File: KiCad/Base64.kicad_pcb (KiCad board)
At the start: 4 copper layers, 25.1 x 81.8 mm, 2 parts, among them J1 1473149-1, U1 68000D

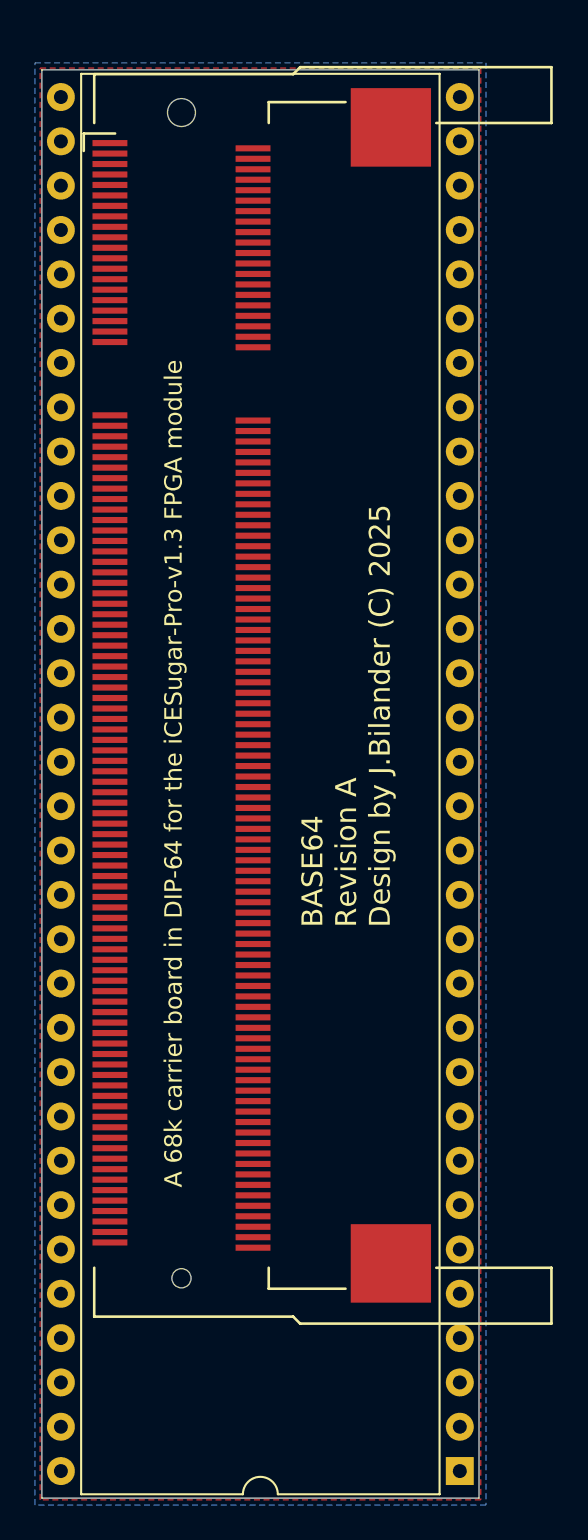
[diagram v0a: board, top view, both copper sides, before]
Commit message: more placement and routing
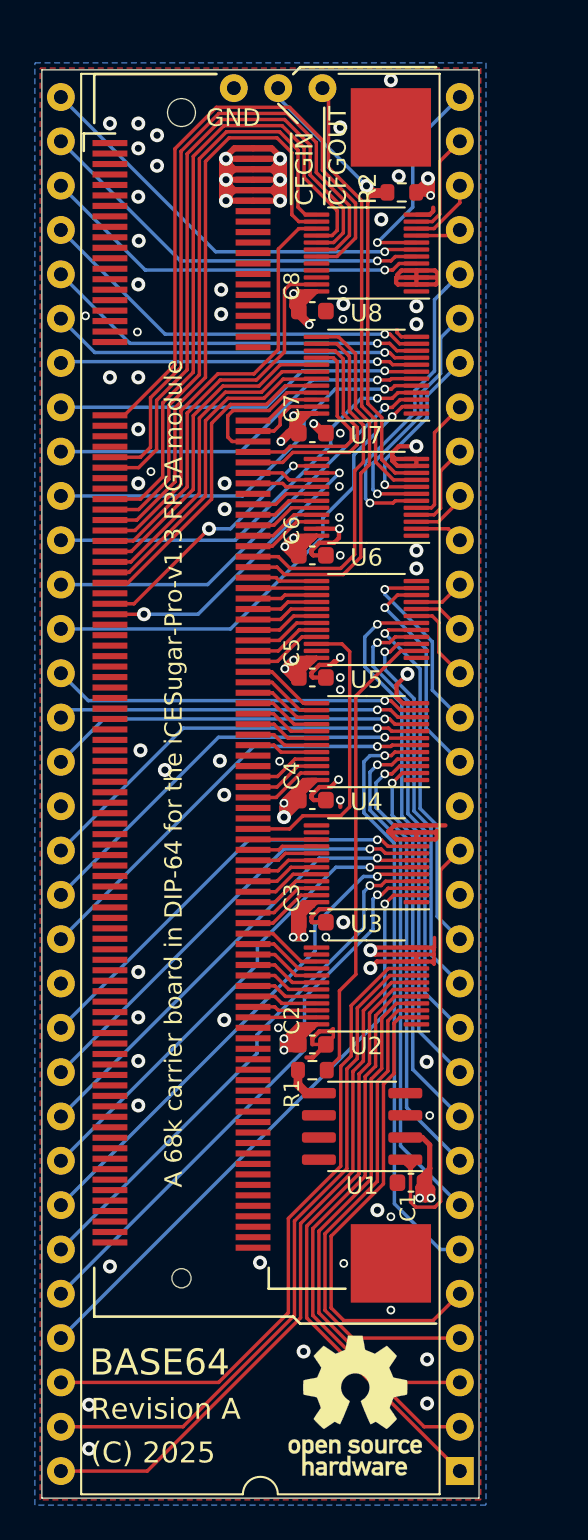
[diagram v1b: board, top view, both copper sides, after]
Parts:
- added C1: 10nF, Capacitor_SMD:C_0603_1608Metric, F.Cu at (110.5, 107.2)
- added C2: 100nF, Capacitor_SMD:C_0603_1608Metric, F.Cu at (104.8, 99.3)
- added C3: 100nF, Capacitor_SMD:C_0603_1608Metric, F.Cu at (104.8, 92.3)
- added C4: 100nF, Capacitor_SMD:C_0603_1608Metric, F.Cu at (104.8, 85.3)
- added C5: 100nF, Capacitor_SMD:C_0603_1608Metric, F.Cu at (104.8, 78.3)
- added C6: 100nF, Capacitor_SMD:C_0603_1608Metric, F.Cu at (104.8, 71.3)
- added C7: 100nF, Capacitor_SMD:C_0603_1608Metric, F.Cu at (104.8, 64.3)
- added C8: 100nF, Capacitor_SMD:C_0603_1608Metric, F.Cu at (104.8, 57.3)
- added J2: Conn_01x03, Connector_PinHeader_2.54mm:PinHeader_1x03_P2.54mm_Horizontal, B.Cu at (105.4, 44.5)
- added R1: 33, Resistor_SMD:R_0603_1608Metric, F.Cu at (104.8, 100.8)
- added R2: R_Small, Resistor_SMD:R_0603_1608Metric, F.Cu at (110.0, 50.5)
- added REF**: OSHW-Logo_7.5x8mm_SilkScreen, Symbol:OSHW-Logo_7.5x8mm_SilkScreen, F.Cu at (107.3, 120.0)
- added REF**: Symbol_CC-Attribution_SilkScreenTop_Small, SF2000:Symbol_CC-Attribution_SilkScreenTop_Small, B.Cu at (101.9, 54.0)
- added REF**: Symbol_CC_SilkScreenTop_Small, SF2000:Symbol_CC_SilkScreenTop_Small, B.Cu at (108.7, 54.0)
- added REF**: Symbol_CC-ShareAlike_SilkScreenTop_Small, SF2000:Symbol_CC-ShareAlike_SilkScreenTop_Small, B.Cu at (95.1, 54.0)
- added REF**: OSHW-Logo_11.4x12mm_SilkScreen, Symbol:OSHW-Logo_11.4x12mm_SilkScreen, B.Cu at (101.9, 112.5)
- added U1: 501MLFT, Package_SO:SOIC-8_3.9x4.9mm_P1.27mm, F.Cu at (107.7, 104.0)
- added U2: SN74CBTD3861DGVR, Package_SO:TSSOP-24_4.4x5mm_P0.4mm, F.Cu at (108.0, 96.0)
- added U3: SN74CBTD3861DGVR, Package_SO:TSSOP-24_4.4x5mm_P0.4mm, F.Cu at (108.0, 89.0)
- added U4: SN74CBTD3861DGVR, Package_SO:TSSOP-24_4.4x5mm_P0.4mm, F.Cu at (108.0, 82.0)
- added U5: SN74CBTD3861DGVR, Package_SO:TSSOP-24_4.4x5mm_P0.4mm, F.Cu at (108.0, 75.0)
- added U6: SN74CBTD3861DGVR, Package_SO:TSSOP-24_4.4x5mm_P0.4mm, F.Cu at (108.0, 68.0)
- added U7: SN74CBTD3861DGVR, Package_SO:TSSOP-24_4.4x5mm_P0.4mm, F.Cu at (108.0, 61.0)
- added U8: SN74CBTD3861DGVR, Package_SO:TSSOP-24_4.4x5mm_P0.4mm, F.Cu at (108.0, 54.0)
- U9: renamed from U1; value 68000D -> 68000_PinHeader
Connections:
- net Net-(J1-Pad101) renamed PL20B
- net Net-(J1-Pad103) renamed PL23A
- net Net-(J1-Pad109) renamed PL23B
- net Net-(J1-Pad111) renamed PL23C
- net Net-(J1-Pad113) renamed PL23D
- net Net-(J1-Pad115) renamed PL26A
- net Net-(J1-Pad116) renamed PT33B
- net Net-(J1-Pad117) renamed PL26B
- net Net-(J1-Pad118) renamed PT27A
- net Net-(J1-Pad119) renamed PL26C
- net Net-(J1-Pad121) renamed PL26D
- net Net-(J1-Pad123) renamed PL32A
- net Net-(J1-Pad125) renamed PL35D
- net Net-(J1-Pad127) renamed PL35A
- net Net-(J1-Pad129) renamed PL32B
- net Net-(J1-Pad131) renamed PL35B
- net Net-(J1-Pad133) renamed PL38C
- net Net-(J1-Pad135) renamed PL38D
- net Net-(J1-Pad137) renamed PL41B
- net Net-(J1-Pad139) renamed PL41D
- net Net-(J1-Pad141) renamed PL41C
- net Net-(J1-Pad143) renamed PL44B
- net Net-(J1-Pad145) renamed PL44A
- net Net-(J1-Pad147) renamed PB4B
- net Net-(J1-Pad149) renamed PB4A
- net Net-(J1-Pad151) renamed PB6B
- net Net-(J1-Pad153) renamed PB6A
- net Net-(J1-Pad155) renamed PB13A
- net Net-(J1-Pad75) renamed PT4A
- net Net-(J1-Pad81) renamed PL5A
- net Net-(J1-Pad83) renamed PL5B
- net Net-(J1-Pad85) renamed PL8A
- net Net-(J1-Pad87) renamed PL2D
- net Net-(J1-Pad89) renamed PL11D
- net Net-(J1-Pad91) renamed PL8B
- net Net-(J1-Pad93) renamed PL14A
- net Net-(J1-Pad95) renamed PL11C
- net Net-(J1-Pad97) renamed PL20A
- net Net-(J1-Pad99) renamed PL14B
- J1 pad 1: Net-(J1-Pad1) -> GND
- J1 pad 10: Net-(J1-Pad10) -> VCC
- J1 pad 100: Net-(J1-Pad100) -> PT51A
- J1 pad 102: Net-(J1-Pad102) -> PT44B
- J1 pad 104: Net-(J1-Pad104) -> PT47A
- J1 pad 105: Net-(J1-Pad105) -> GND
- J1 pad 106: Net-(J1-Pad106) -> GND
- J1 pad 107: Net-(J1-Pad107) -> GND
- J1 pad 108: Net-(J1-Pad108) -> GND
- J1 pad 11: Net-(J1-Pad11) -> GND
- J1 pad 110: Net-(J1-Pad110) -> PT38B
- J1 pad 112: Net-(J1-Pad112) -> PT40A
- J1 pad 114: Net-(J1-Pad114) -> PT35A
- J1 pad 12: Net-(J1-Pad12) -> VCC
- J1 pad 120: Net-(J1-Pad120) -> PT24B
- J1 pad 122: Net-(J1-Pad122) -> PT22A
- J1 pad 124: Net-(J1-Pad124) -> PT20B
- J1 pad 126: Net-(J1-Pad126) -> PT15A
- J1 pad 128: Net-(J1-Pad128) -> PT13B
- J1 pad 130: Net-(J1-Pad130) -> PT11A
- J1 pad 132: Net-(J1-Pad132) -> PT9B
- J1 pad 134: Net-(J1-Pad134) -> PL2C
- J1 pad 136: Net-(J1-Pad136) -> PT9A
- J1 pad 138: Net-(J1-Pad138) -> PL5C
- J1 pad 140: Net-(J1-Pad140) -> PL8C
- J1 pad 142: Net-(J1-Pad142) -> PL5D
- J1 pad 144: Net-(J1-Pad144) -> PL11B
- J1 pad 146: Net-(J1-Pad146) -> PL14C
- J1 pad 148: Net-(J1-Pad148) -> PL14D
- J1 pad 150: Net-(J1-Pad150) -> PL17C
- J1 pad 152: Net-(J1-Pad152) -> PL20C
- J1 pad 154: Net-(J1-Pad154) -> PL29A
- J1 pad 156: Net-(J1-Pad156) -> PL20D
- J1 pad 157: Net-(J1-Pad157) -> GND
- J1 pad 158: Net-(J1-Pad158) -> GND
- J1 pad 199: Net-(J1-Pad199) -> GND
- J1 pad 2: Net-(J1-Pad2) -> VCC
- J1 pad 200: Net-(J1-Pad200) -> GND
- J1 pad 3: Net-(J1-Pad3) -> GND
- J1 pad 39: Net-(J1-Pad39) -> GND
- J1 pad 4: Net-(J1-Pad4) -> VCC
- J1 pad 40: Net-(J1-Pad40) -> GND
- J1 pad 41: Net-(J1-Pad41) -> PT29B
- J1 pad 42: Net-(J1-Pad42) -> PR47C
- J1 pad 44: Net-(J1-Pad44) -> PR47D
- J1 pad 46: Net-(J1-Pad46) -> PR44D
- J1 pad 48: Net-(J1-Pad48) -> PR41A
- J1 pad 49: Net-(J1-Pad49) -> PT35B
- J1 pad 5: Net-(J1-Pad5) -> GND
- J1 pad 50: Net-(J1-Pad50) -> PR38A
- J1 pad 51: Net-(J1-Pad51) -> PT29A
- J1 pad 52: Net-(J1-Pad52) -> PR38B
- J1 pad 54: Net-(J1-Pad54) -> PR44C
- J1 pad 55: Net-(J1-Pad55) -> GND
- J1 pad 56: Net-(J1-Pad56) -> GND
- J1 pad 57: Net-(J1-Pad57) -> PT27B
- J1 pad 58: Net-(J1-Pad58) -> PR35C
- J1 pad 59: Net-(J1-Pad59) -> PT18B
- J1 pad 6: Net-(J1-Pad6) -> VCC
- J1 pad 60: Net-(J1-Pad60) -> PR32C
- J1 pad 61: Net-(J1-Pad61) -> PT22B
- J1 pad 62: Net-(J1-Pad62) -> PR29C
- J1 pad 63: Net-(J1-Pad63) -> PT18A
- J1 pad 64: Net-(J1-Pad64) -> PR20D
- J1 pad 65: Net-(J1-Pad65) -> PT15B
- J1 pad 66: Net-(J1-Pad66) -> PR29A
- J1 pad 67: Net-(J1-Pad67) -> PT6B
- J1 pad 68: Net-(J1-Pad68) -> PR20C
- J1 pad 69: Net-(J1-Pad69) -> PT11B
- J1 pad 7: Net-(J1-Pad7) -> GND
- J1 pad 70: Net-(J1-Pad70) -> PR17C
- J1 pad 71: Net-(J1-Pad71) -> PT6A
- J1 pad 72: Net-(J1-Pad72) -> PR14D
- J1 pad 73: Net-(J1-Pad73) -> PT4B
- J1 pad 74: Net-(J1-Pad74) -> PR17B
- J1 pad 76: Net-(J1-Pad76) -> PR14C
- J1 pad 77: Net-(J1-Pad77) -> PL2A
- J1 pad 78: Net-(J1-Pad78) -> PR11B
- J1 pad 79: Net-(J1-Pad79) -> PL2B
- J1 pad 8: Net-(J1-Pad8) -> VCC
- J1 pad 80: Net-(J1-Pad80) -> PR5D
- J1 pad 82: Net-(J1-Pad82) -> PR8C
- J1 pad 84: Net-(J1-Pad84) -> PR5C
- J1 pad 86: Net-(J1-Pad86) -> PT62B
- J1 pad 88: Net-(J1-Pad88) -> PT58B
- J1 pad 9: Net-(J1-Pad9) -> GND
- J1 pad 90: Net-(J1-Pad90) -> PT62D
- J1 pad 92: Net-(J1-Pad92) -> PT62A
- J1 pad 94: Net-(J1-Pad94) -> PT58D
- J1 pad 96: Net-(J1-Pad96) -> PT58A
- J1 pad 98: Net-(J1-Pad98) -> PT49B
- J1 pad MP1: Net-(J1-PadMP1) -> GND
- J1 pad MP2: Net-(J1-PadMP2) -> GND
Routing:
- net VCC: track 0.00 -> 121.7 mm, vias 0 -> 24
- net GND: track 0.00 -> 65.2 mm, vias 0 -> 71
- net D5: track 0.00 -> 40.2 mm
- net D6: track 0.00 -> 39.3 mm
- net D7: track 0.00 -> 38.4 mm
- net PT35B: track 0.00 -> 37.9 mm
- net PT27B: track 0.00 -> 37.1 mm
- net PT29A: track 0.00 -> 36.8 mm
- net PT29B: track 0.00 -> 36.6 mm
- net PT22B: track 0.00 -> 34.7 mm
- net D4: track 0.00 -> 34.6 mm
- net D8: track 0.00 -> 34.6 mm, vias 0 -> 1
- net PT18B: track 0.00 -> 34.4 mm
- net AS: track 0.00 -> 34.1 mm, vias 0 -> 1
- net D9: track 0.00 -> 32.8 mm, vias 0 -> 1
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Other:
- board text added: "(C) 2025"
- board text added: "BASE64"
- board text added: "CC BY-SA 4.0"
- board text added: "Design by J.Bilander"
- board text added: "GND"
- board text added: "JLCJLCJLCJLC"
- board text added: "Revision A"
- board text added: "~CFGIN"
- board text added: "~CFGOUT"
- board text removed: "BASE64 Revision A Design by J.Bilander (C) 2025"

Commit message: silkscreen fixes, adding a dot to indicate pin 1 on all IC footprints
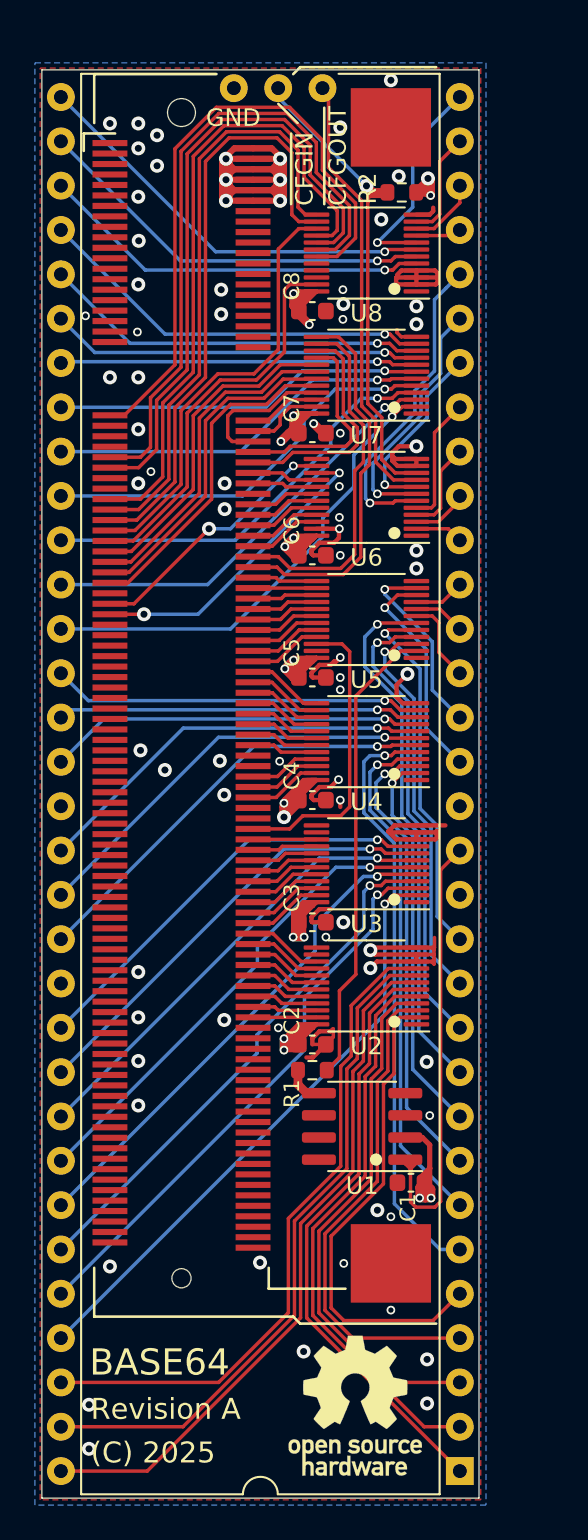
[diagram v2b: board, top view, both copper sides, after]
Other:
- board text removed: "A 68k carrier board in DIP-64 for the iCESugar-Pro-v1.3 FPGA module"

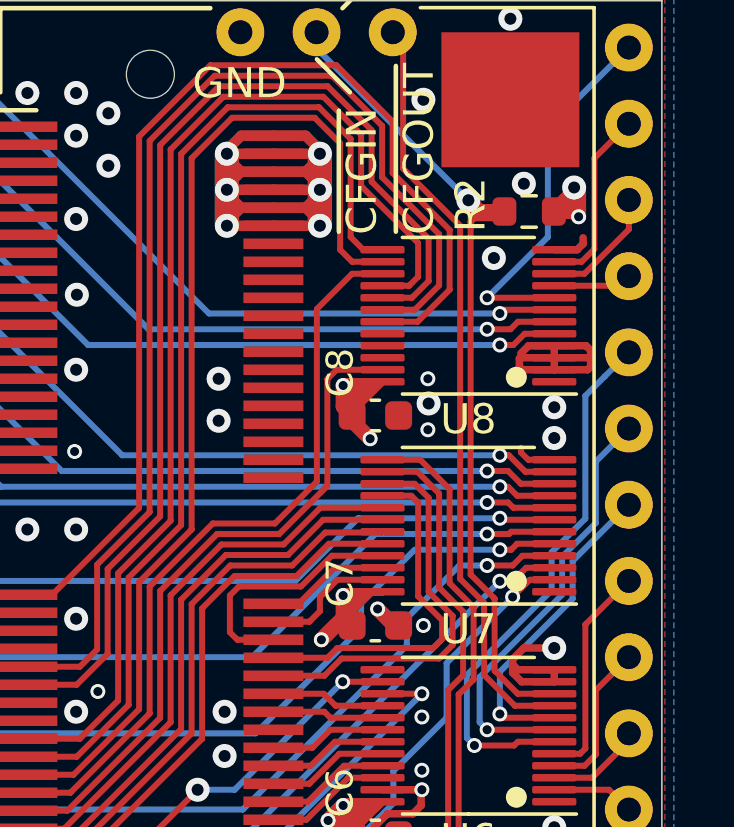
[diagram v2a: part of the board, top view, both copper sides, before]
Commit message: Add value (10k) to R2 pull-up resistor and some small routing improvements
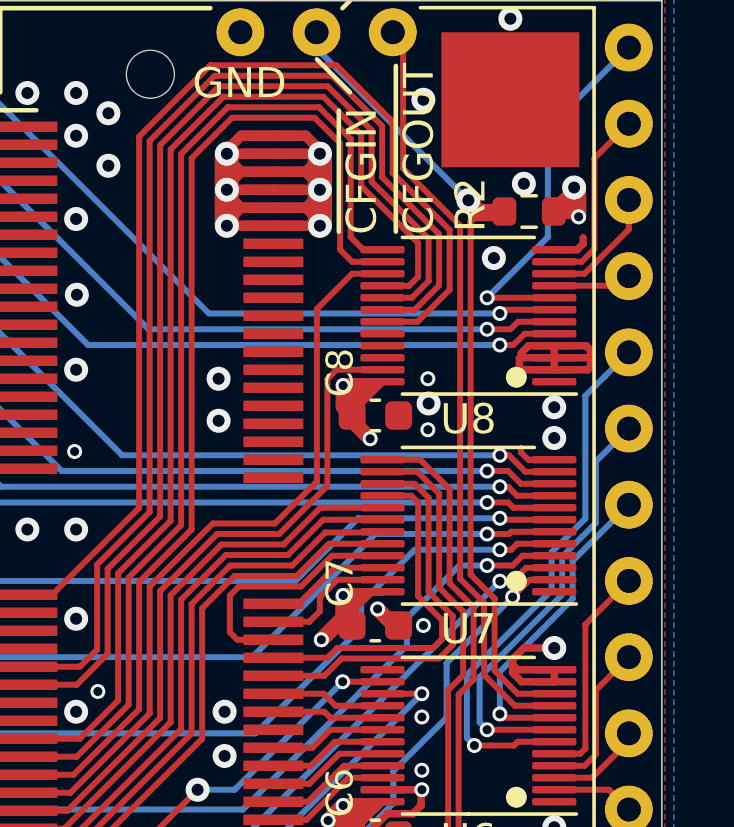
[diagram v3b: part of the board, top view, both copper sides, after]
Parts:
- R2: value R_Small -> 10k
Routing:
- net VCC: track 121.7 -> 124.5 mm
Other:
- rule via_min_size: 0.4 -> 0.5
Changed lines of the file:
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@@
     (thickness 1.6)
     (drawings 18)
-    (tracks 1173)
+    (tracks 1177)
     (zones 0)
     (modules 26)
@@
   )
   (setup
-    (last_trace_width 0.1524)
+    (last_trace_width 0.5)
     (user_trace_width 0.2)
     (user_trace_width 0.25)
@@
     (via_size 0.8)
     (via_drill 0.4)
-    (via_min_size 0.4)
+    (via_min_size 0.5)
     (via_min_drill 0.25)
     (user_via 0.4 0.25)
@@
     (uvia_drill 0.1)
     (uvias_allowed no)
-    (uvia_min_size 0.2)
+    (uvia_min_size 0.3)
     (uvia_min_drill 0.1)
     (edge_width 0.05)
@@
       (effects (font (size 1 1) (thickness 0.15)))
     )
-    (fp_text value R_Small (at 0 1.43) (layer F.Fab) hide
+    (fp_text value 10k (at 0 1.43) (layer F.Fab) hide
       (effects (font (size 1 1) (thickness 0.15)))
     )
@@
   (segment (start 111.625 50.65) (end 111.625 49.825) (width 0.5) (layer F.Cu) (net 2))
   (segment (start 103.275 70.775) (end 103.775 70.275) (width 0.5) (layer B.Cu) (net 2))
+  (segment (start 111.625 49.825) (end 111.475 49.675) (width 0.5) (layer B.Cu) (net 2))
+  (segment (start 111.625 50.65) (end 111.625 49.825) (width 0.5) (layer B.Cu) (net 2))
+  (segment (start 103.775 64.025) (end 103.05 64.75) (width 0.5) (layer B.Cu) (net 2))
+  (segment (start 103.775 63.275) (end 103.775 64.025) (width 0.5) (layer B.Cu) (net 2))
   (via (at 108.575 53.35) (size 0.5) (drill 0.3) (layers F.Cu B.Cu) (net 3))
   (segment (start 110.8125 53.35) (end 108.575 53.35) (width 0.2) (layer F.Cu) (net 3))

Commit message: Fixed typo on CFGOUT net and corrected signal direction on many nets
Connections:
- net CFOUT renamed CFGOUT

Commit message: Small silkscreen fix on underside
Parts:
- moved REF** 0.20 mm to (101.9, 53.8)
- moved REF** 0.20 mm to (108.7, 53.8)
- moved REF** 0.20 mm to (95.1, 53.8)

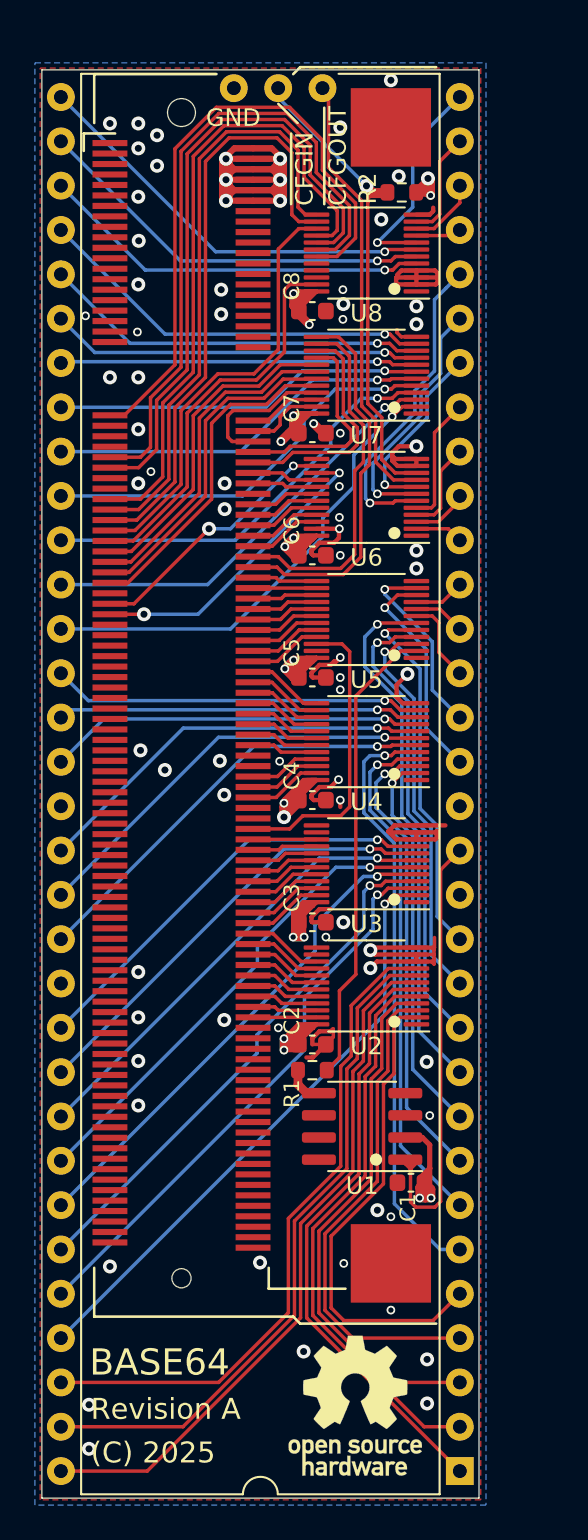
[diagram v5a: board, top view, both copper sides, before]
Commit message: Add a 74AHCT1G17 buffering the raw 7 MHz clk and fanout to the 501 PLL (U1) and a pin in the CBTD (U6) that propagates to PL23A (J1 on the FPGA)
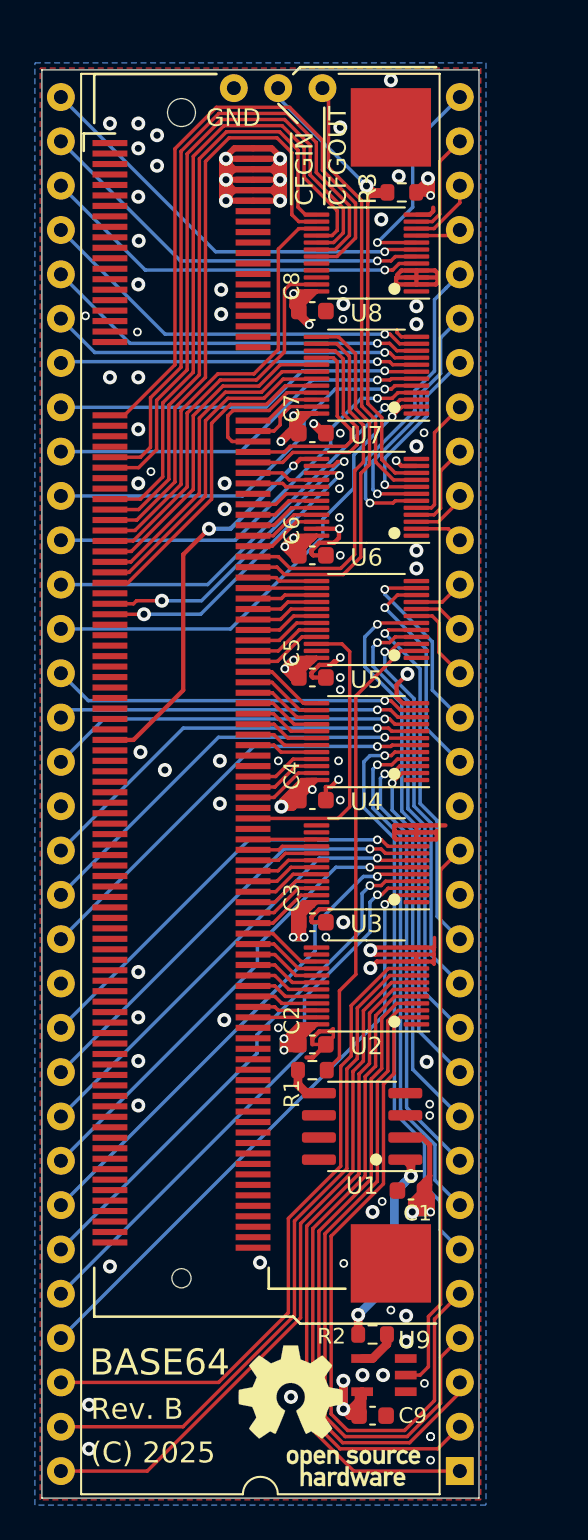
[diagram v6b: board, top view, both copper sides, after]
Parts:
- added C9: 100nF, Capacitor_SMD:C_0603_1608Metric, F.Cu at (108.3, 120.6)
- added R2: 33, Resistor_SMD:R_0603_1608Metric, F.Cu at (108.3, 115.9)
- added U9: 74AHCT1G17, Base64:SOT95P275X110-5N, F.Cu at (109.0, 118.2)
- moved REF** 3.74 mm to (103.6, 120.5)
- moved C1 0.45 mm to (110.5, 107.7)
- renumbered R2 to R3, U9 to U10
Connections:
- U10 pad 15: CLK -> RAW_CLK
- U5 pad 22: PT24B -> PT27A
- U6 pad 11: GND -> CLK
- U6 pad 13: Net-(U6-Pad13) -> PL23A
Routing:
- net RAW_CLK: track 0.00 -> 31.8 mm
- net CLK: track 27.5 -> 56.4 mm, vias 0 -> 3
- net PL23A: track 0.00 -> 23.1 mm, vias 0 -> 2
- net PT24B: track 17.0 -> 0.00 mm
- net PT27A: track 0.00 -> 16.8 mm
- net VCC: track 124.5 -> 136.6 mm, vias 24 -> 26
- net D0: track 27.5 -> 39.1 mm
- net D1: track 28.4 -> 38.1 mm
- net GND: track 65.2 -> 57.9 mm, vias 71 -> 80
- net D2: track 30.4 -> 37.2 mm
- net D3: track 32.5 -> 37.1 mm
- net D4: track 34.6 -> 38.2 mm
- net PL2A: track 15.1 -> 18.5 mm
- net /CLK_BUF: track 0.00 -> 2.32 mm
- net AS: track 34.1 -> 33.5 mm
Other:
- board text added: "Rev. B"
- board text removed: "Revision A"
